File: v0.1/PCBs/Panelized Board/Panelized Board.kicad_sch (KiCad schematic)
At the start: 87 parts, among them J1 FFC Connector, J1 USB C Connector, J2 DuPont Connector, J2 FFC Connector, J2 JTAG_TC2030, J3 JST Connector, J4 DuPont Connector, J4 JST Connector, SW1 Boot, U1 XC6206, U2 USBLC6-2SC6, U3 RP2040, U4 W25Q128JVS, Y1 12MHz

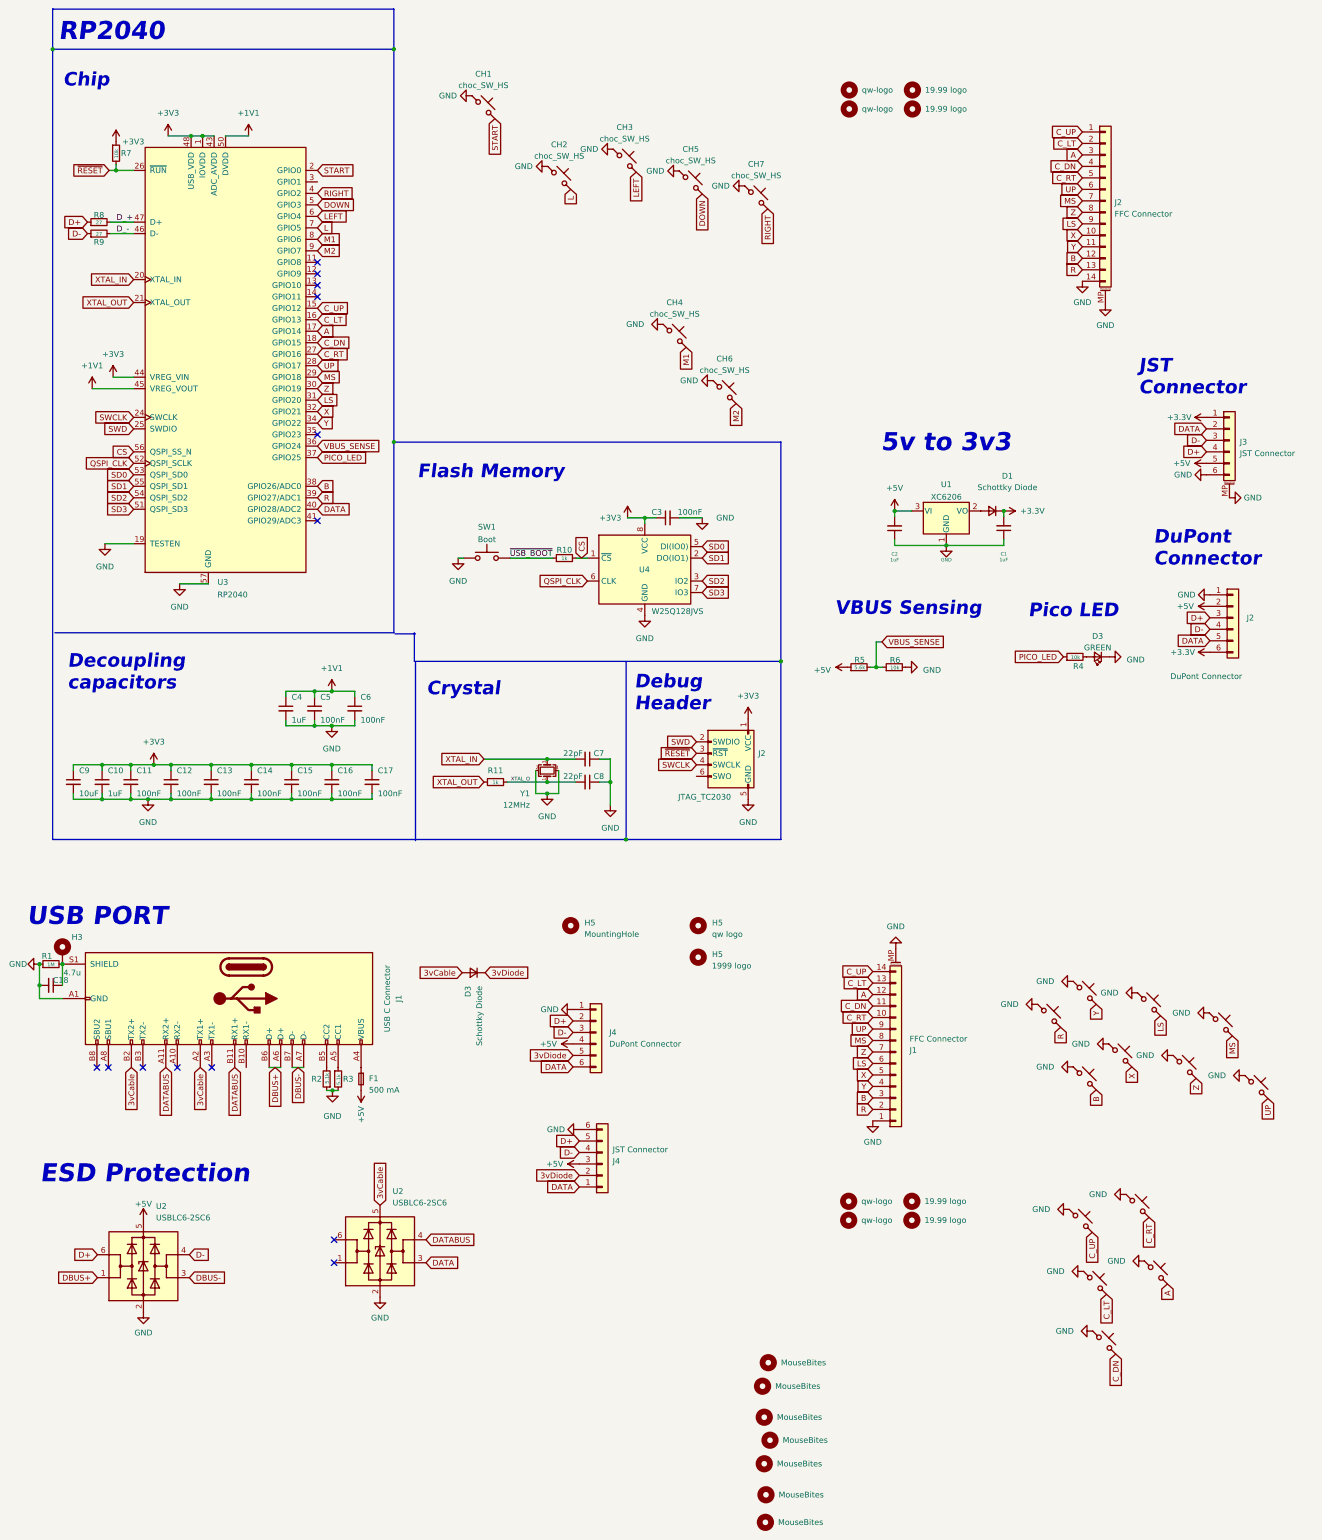
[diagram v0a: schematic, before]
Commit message: Adjusted choc to the preferred footprint
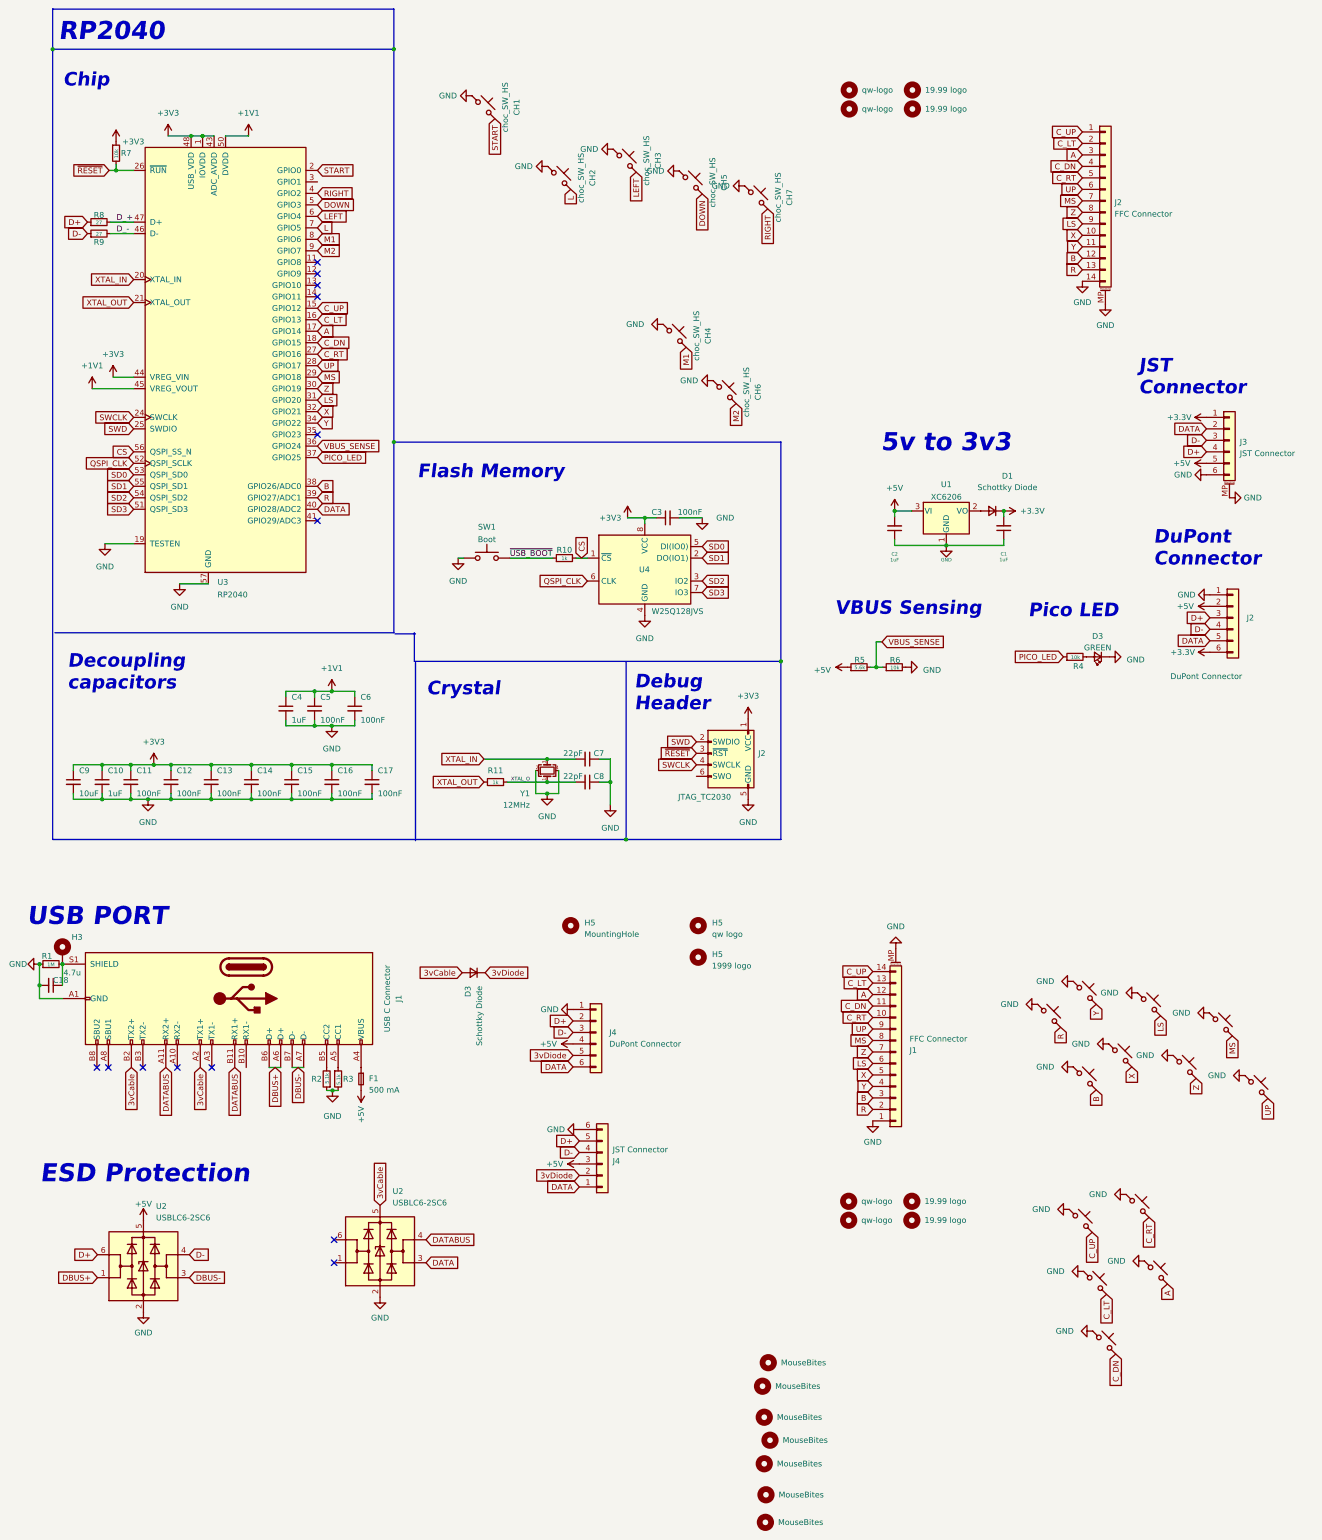
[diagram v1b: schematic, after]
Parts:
- CH1, CH10, CH11, CH12, CH13, CH14, CH15, CH16, CH17, CH18, CH19, CH2, CH20, CH3, CH4, CH5, CH6, CH7, CH8, CH9: footprint PCM_marbastlib-choc:SW_choc_v1_HS_1u -> PCBs:Kailh_socket_PG1350
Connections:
- net A: now also CH17.1; no longer CH17.2
- net B: now also CH11.1; no longer CH11.2
- net C_DN: now also CH13.1; no longer CH13.2
- net C_LT: now also CH12.1; no longer CH12.2
- net C_RT: now also CH15.1; no longer CH15.2
- net C_UP: now also CH9.1; no longer CH9.2
- net DOWN: now also CH5.1; no longer CH5.2
- net GND: now also CH1.2, CH10.2, CH11.2, CH12.2, CH13.2, CH14.2, CH15.2, CH16.2, CH17.2, CH18.2, CH19.2, CH2.2, CH20.2, CH3.2, CH4.2, CH5.2, CH6.2, CH7.2, CH8.2, CH9.2; no longer CH1.1, CH10.1, CH11.1, CH12.1, CH13.1, CH14.1, CH15.1, CH16.1, CH17.1, CH18.1, CH19.1, CH2.1, CH20.1, CH3.1, CH4.1, CH5.1, CH6.1, CH7.1, CH8.1, CH9.1
- net L: now also CH2.1; no longer CH2.2
- net LEFT: now also CH3.1; no longer CH3.2
- net LS: now also CH16.1; no longer CH16.2
- net M1: now also CH4.1; no longer CH4.2
- net M2: now also CH6.1; no longer CH6.2
- net MS: now also CH19.1; no longer CH19.2
- net R: now also CH8.1; no longer CH8.2
- net RIGHT: now also CH7.1; no longer CH7.2
- net START: now also CH1.1; no longer CH1.2
- net UP: now also CH20.1; no longer CH20.2
- net X: now also CH14.1; no longer CH14.2
- net Y: now also CH10.1; no longer CH10.2
- net Z: now also CH18.1; no longer CH18.2
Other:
- moved on the sheet: CH1, CH2, CH3, CH4, CH5, CH6, CH7

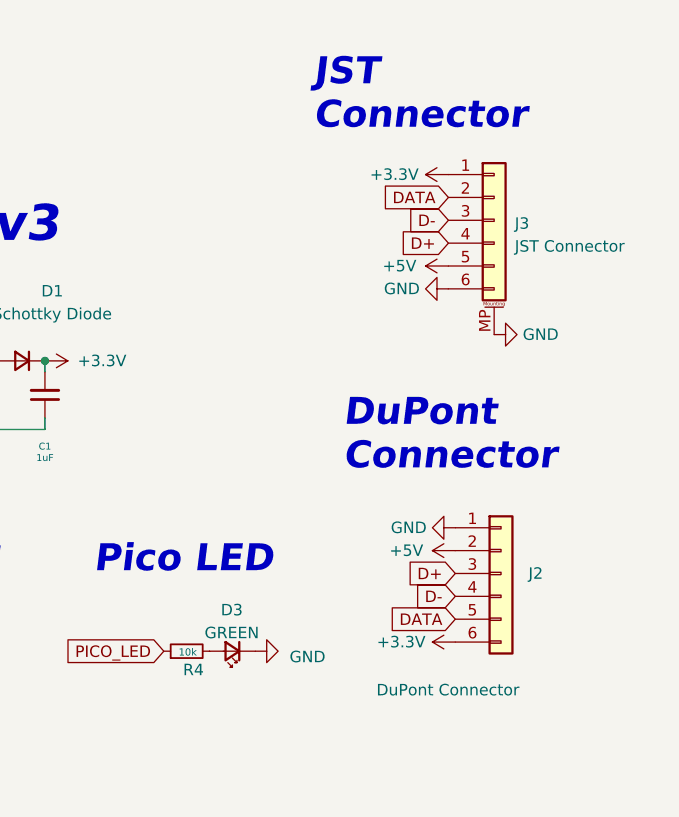
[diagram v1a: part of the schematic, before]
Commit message: Adjusted daughterboard pinout and drill hole error on right hand
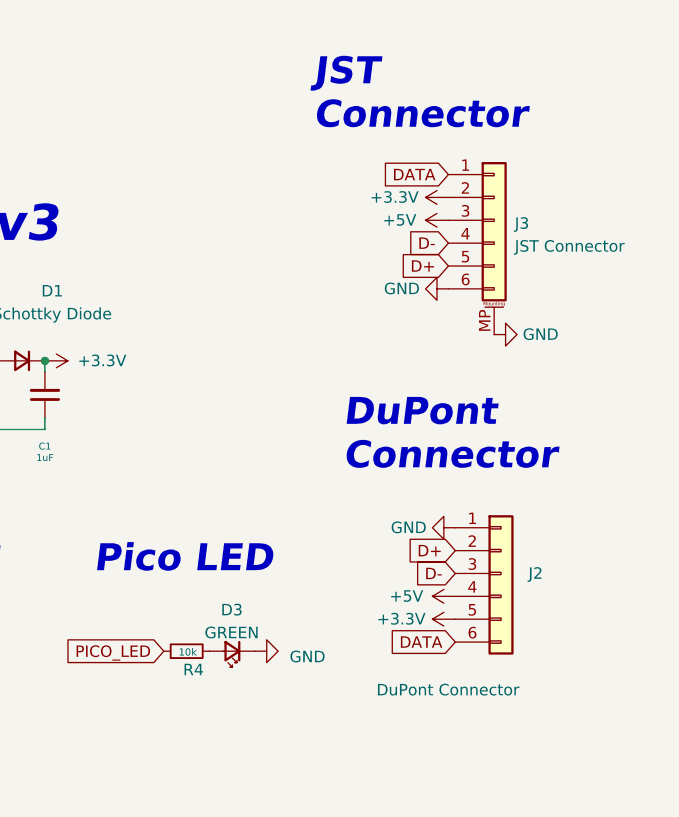
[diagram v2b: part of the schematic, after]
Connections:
- net +3V3: now also J2.5 (Pin_5), J3.2 (Pin_2); no longer J2.6 (Pin_6), J3.1 (Pin_1)
- net +5V: now also J2.4 (Pin_4), J3.3 (Pin_3); no longer J2.2 (Pin_2), J3.5 (Pin_5)
- net D+: now also J2.2 (Pin_2), J3.5 (Pin_5); no longer J2.3 (Pin_3), J3.4 (Pin_4)
- net D-: now also J2.3 (Pin_3), J3.4 (Pin_4); no longer J2.4 (Pin_4), J3.3 (Pin_3)
- net DATA: now also J2.6 (Pin_6), J3.1 (Pin_1); no longer J2.5 (Pin_5), J3.2 (Pin_2)
